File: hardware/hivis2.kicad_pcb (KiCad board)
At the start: 2 copper layers, 70 x 50 mm, 15 parts, among them J1 BME_688_Module, J2 INMP_441, J3 OLED Display, J4 J5019_Module, J5 JST_PH2.0_BATT, SW1 SW_Push

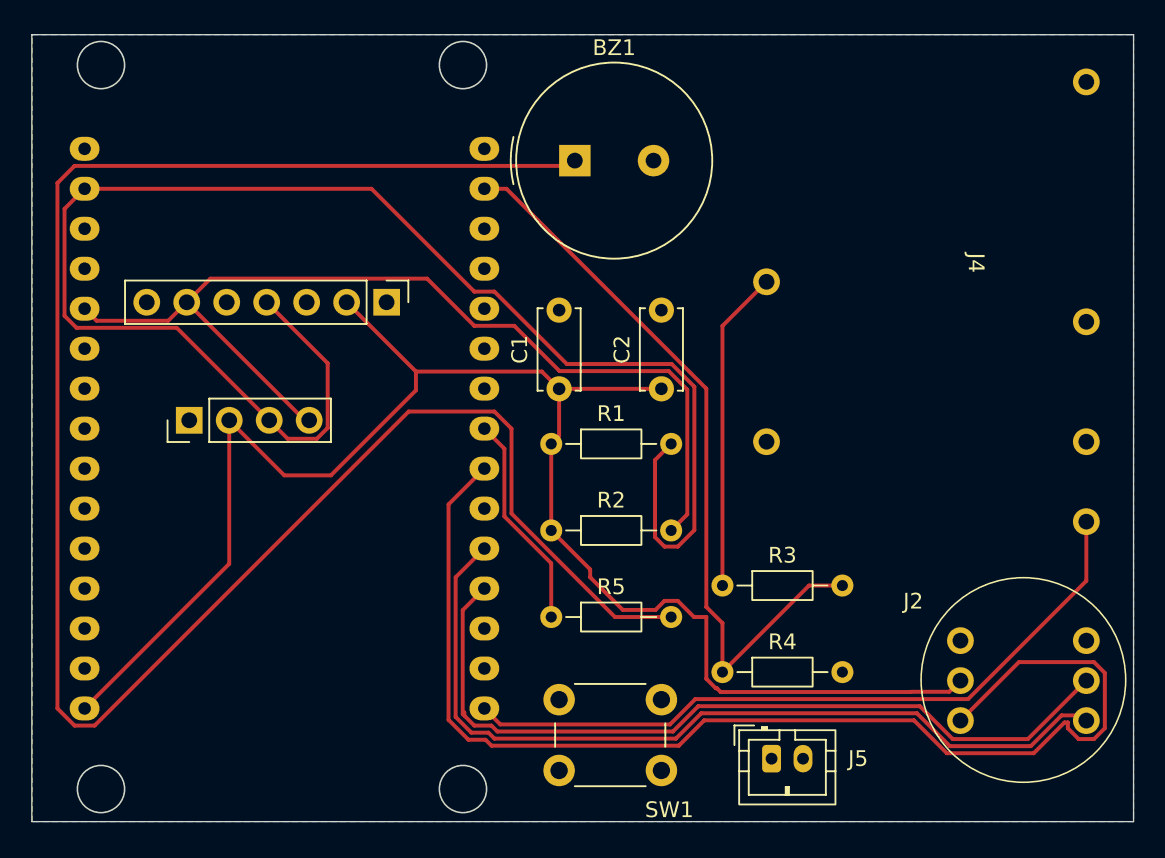
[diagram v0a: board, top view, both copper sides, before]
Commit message: Add SMD variant: schematic, Gerbers, BOM, and production files
Updated KiCad project files with SMD components. New files:
- hivis2smd.kicad_sch — SMD schematic
- gerbers/smd/ — SMD Gerber set + zip
- gerbers/hivistht.zip — THT Gerber zip
- production/ — BOM, positions, netlist, and fabrication zip
- hivis2smdBOM.csv, top/bottom position CSVs

Co-Authored-By: Claude Sonnet 4.6 <noreply@anthropic.com>
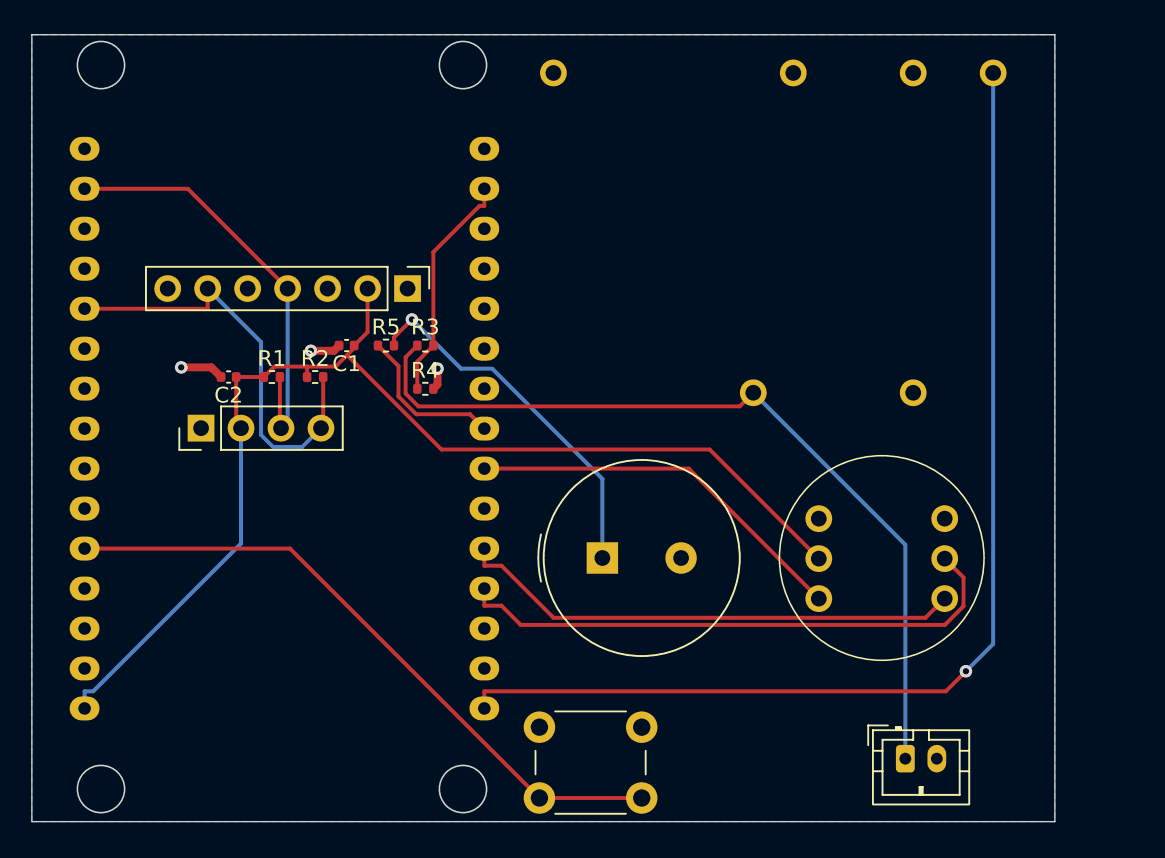
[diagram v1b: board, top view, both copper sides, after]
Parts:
- C1, C2: footprint Capacitor_THT:C_Disc_D5.0mm_W2.5mm_P5.00mm -> Capacitor_SMD:C_0402_1005Metric
- J5: value JST_PH2.0_BATT -> BATT JST
- R1, R2, R3, R4, R5: footprint Resistor_THT:R_Axial_DIN0204_L3.6mm_D1.6mm_P7.62mm_Horizontal -> Resistor_SMD:R_0402_1005Metric
- moved J4 33.9 mm to (138.6, 25.9), turned to 0 degrees
- moved C2 27.5 mm to (118.0, 45.2), turned to 180 degrees
- moved R4 26.1 mm to (130.5, 46.0)
- moved BZ1 25.3 mm to (141.8, 56.8)
- moved R3 24.3 mm to (130.5, 43.2)
- moved R5 20.2 mm to (128.0, 43.2)
- moved R1 18.3 mm to (120.8, 45.2)
- moved R2 17.9 mm to (123.5, 45.2)
- moved C1 13.8 mm to (125.5, 43.2), turned to 180 degrees
- moved J2 11.9 mm to (155.5, 54.2)
- moved J5 8.50 mm to (161.0, 69.5)
- moved SW1 2.15 mm to (144.2, 72.0)
- moved J1 1.59 mm to (121.8, 47.2)
- moved J3 0.90 mm to (116.2, 48.5)
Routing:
- net Net-(BZ1-+): track 123.1 -> 23.5 mm, vias 0 -> 1
- net /SCL: track 101.0 -> 27.8 mm
- net /I2S_SD: track 77.1 -> 24.7 mm
- net /BTN: track 0.00 -> 42.0 mm
- net /SDA: track 62.9 -> 27.7 mm
- net /BAT_ADC: track 47.7 -> 14.7 mm
- net +BATT: track 20.5 -> 53.4 mm
- net +3V3: track 104.0 -> 74.0 mm
- net +5V: track 46.2 -> 70.9 mm, vias 0 -> 1
- net /I2S_SCK: track 54.6 -> 32.2 mm
- net /I2S_WS: track 51.9 -> 36.1 mm
- net GND: track 0.00 -> 6.61 mm, vias 10 -> 3
- net /Buzzer: track 13.7 -> 10.1 mm
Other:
- board size 70 x 50 mm -> 65 x 50 mm
